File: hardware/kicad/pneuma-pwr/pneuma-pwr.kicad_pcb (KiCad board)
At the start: 4 copper layers, 41 x 39 mm, 75 parts, among them J1 USB-C, J2 BATTERY, J3 U.FL, J4 nanoSIM, J5 TO_MAIN, Q1 2N7002, Q2 2N7002, U1 USBLC6-2P6, U2 BQ24074RGTR, U3 LC709203FQH-01TWG, U4 FSUSB42MUX, U5 EG800Q-NA, U6 TXB0104RGYR, U7 TXB0104RGYR, U8 ESDA6V1-5SC6, U9 AT42QT1011-MAH

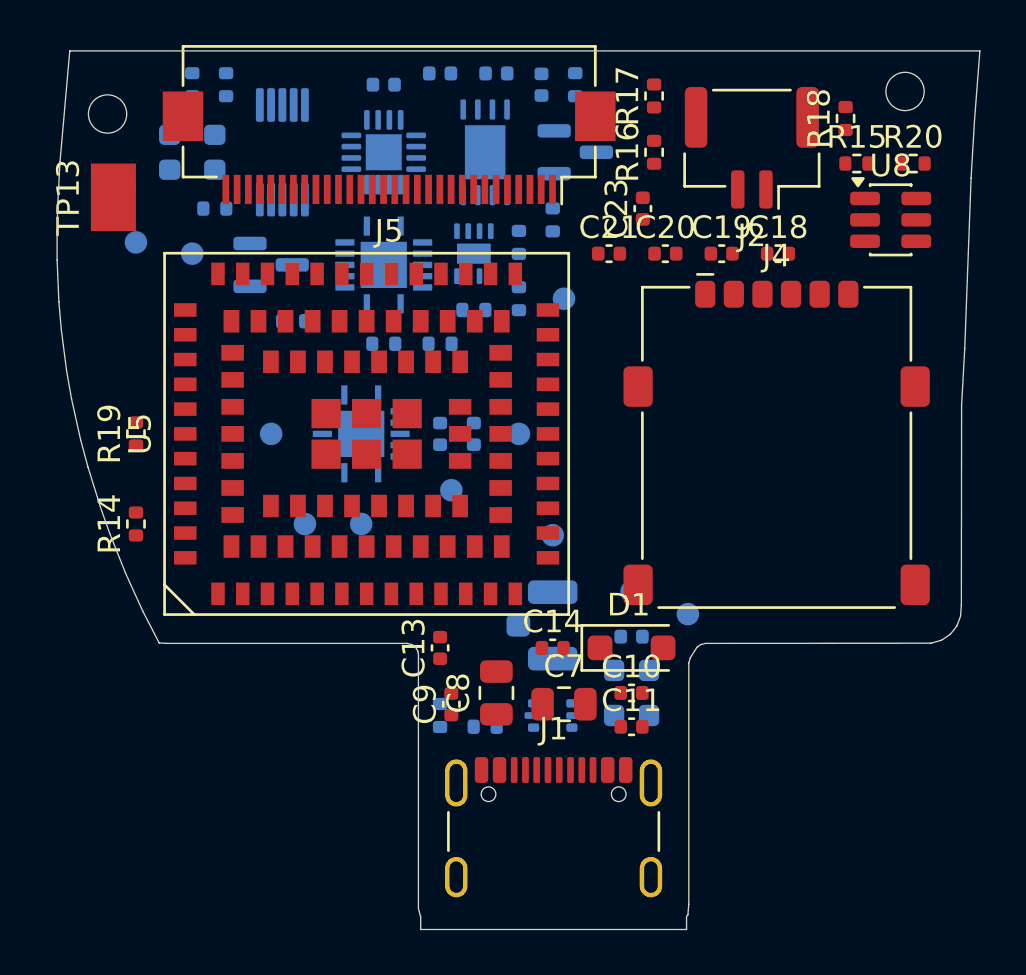
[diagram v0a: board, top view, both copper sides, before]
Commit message: Move the touch pad under the camera bump, per the intended interaction
The touch area was over the battery, following K's "thin touch area" on the
lower front face.  It should sit ~10 mm below the camera bump, where a finger
lands: a 24 x 16 mm electrode at x -12..12, y -12..4 on the front membrane.

Consequences carried through:
- the AT42QT1011 front-end moves from PNM-PWR to PNM-MAIN beside the nRF, so
  the electrode run is short and TOUCH_OUT no longer crosses the FFC.  FFC pin
  27 becomes GND
- the electrode contacts PNM-MAIN TP11 at (11.0, 4.6)
- the speaker moves +2.2 mm in y to clear the pad.  It stays the 1 W 15 mm
  round part: the only sub-15 mm options are 5 mW earpiece receivers, and the
  15x11 alternative is 0.3 W (~5 dB quieter)
- the copper spreader keep-out follows the pad

Sensitivity is now the open question: the battery pouch is 1-2 mm behind the
pad's lower half and the speaker sits just above it.  Both are in REV-A.md as
bench-tuning items (Cs, and a foam spacer to hold the electrode off the metal).
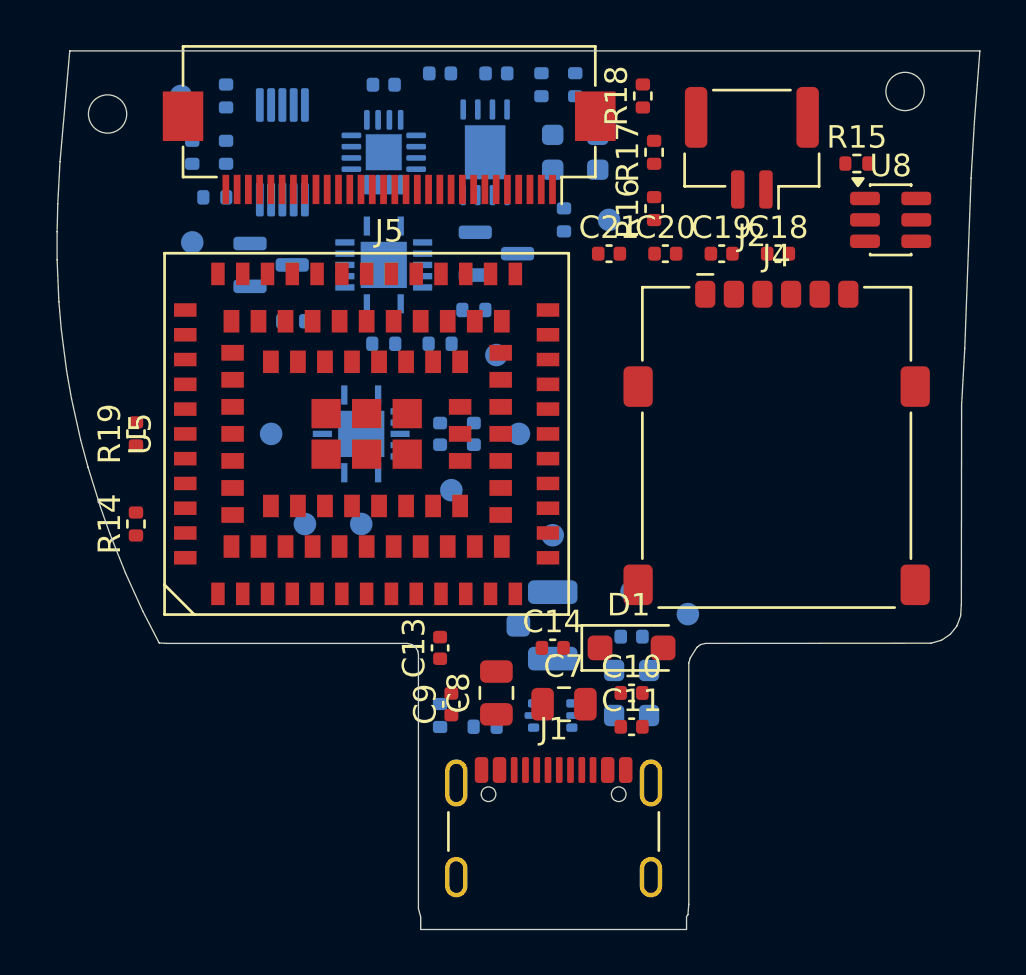
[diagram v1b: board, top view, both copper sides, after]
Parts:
- removed C22: 100n, C_0402_1005Metric
- removed C23: 22n, C_0402_1005Metric
- removed R20: 4.7k, R_0402_1005Metric
- removed TP13: TOUCH_E, SpringPad_3.0x2.0mm
- removed U9: AT42QT1011-MAH, DFN-8-1EP_2x2mm_P0.5mm_EP0.9x1.5mm
- moved TP2 21.0 mm to (102.5, 127.3)
- moved C3 19.0 mm to (102.0, 124.3)
- moved R9 15.9 mm to (95.0, 132.8), turned to 0 degrees
- moved R12 15.5 mm to (85.5, 121.8)
- moved C2 15.0 mm to (100.0, 124.3)
- moved Q2 14.4 mm to (87.5, 129.3)
- moved R11 14.0 mm to (99.5, 121.3)
- moved R10 13.6 mm to (85.5, 124.3)
- moved R8 13.0 mm to (101.0, 121.3), turned to 90 degrees
- moved R13 12.5 mm to (85.0, 126.3)
- moved R3 12.3 mm to (96.5, 131.3)
- moved Q1 10.0 mm to (97.5, 128.8)
- moved R18 9.06 mm to (104.0, 121.8)
- moved R4 8.75 mm to (84.0, 124.3), turned to 90 degrees
- moved TP10 7.02 mm to (83.5, 121.8)
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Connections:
- J5 pad 27: TOUCH_OUT -> GND
